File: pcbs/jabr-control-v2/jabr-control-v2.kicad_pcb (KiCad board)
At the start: 6 copper layers, 70 x 80 mm, 245 parts, among them J10001 ARJM11D7-502-AB-EW2, J10002 TYPE-C-31-M-12, J1001 48406-0003, J1002 FH12-22S-0.5SH, J1501 FH12-22S-0.5SH, J1502 FH12-22S-0.5SH, J201 JST-SH-4-Vertical, J4001 MDT320E0X001, J6001 MSPE-J2L0-x00, J9001 43045-0201, Q2602 DMN21D2UFB-7B, SW202 TS20-42-25-WT-160-SMT-TR, U1001 AP22653FDZ-7, U1002 PESD4USB3BTTS-QX, U1003 PESD4USB3BTTS-QX, U1004 PESD4USB3BTTS-QX, U1005 PESD4USB3BTTS-QX, U1201 TPS259472ARPWR, U1301 MAX20004AFOC/VY+T, U1401 TPS62290TDRVRQ1, U1501 TPS62290TDRVRQ1, U201 NX3DV221TKX, U2401 PESD4USB3BTTS-QX, U2402 PESD4USB3BTTS-QX, U301 TVS3301DRBR, U302 TPS26600RHFR, U303 PI7C9X2G304SL, U3801 TPS62290TDRVRQ1, U401 LMQ66430MC3RXBRQ1, U402 TPS7B8133QDRVRQ1, U403 TPS2116DRL, U5001 LAN7431_YXX, U8001 LAN8870, Y401 ASEK-32.768KHZ-LRT, Y8001 XRCGB25M000F3A16R0

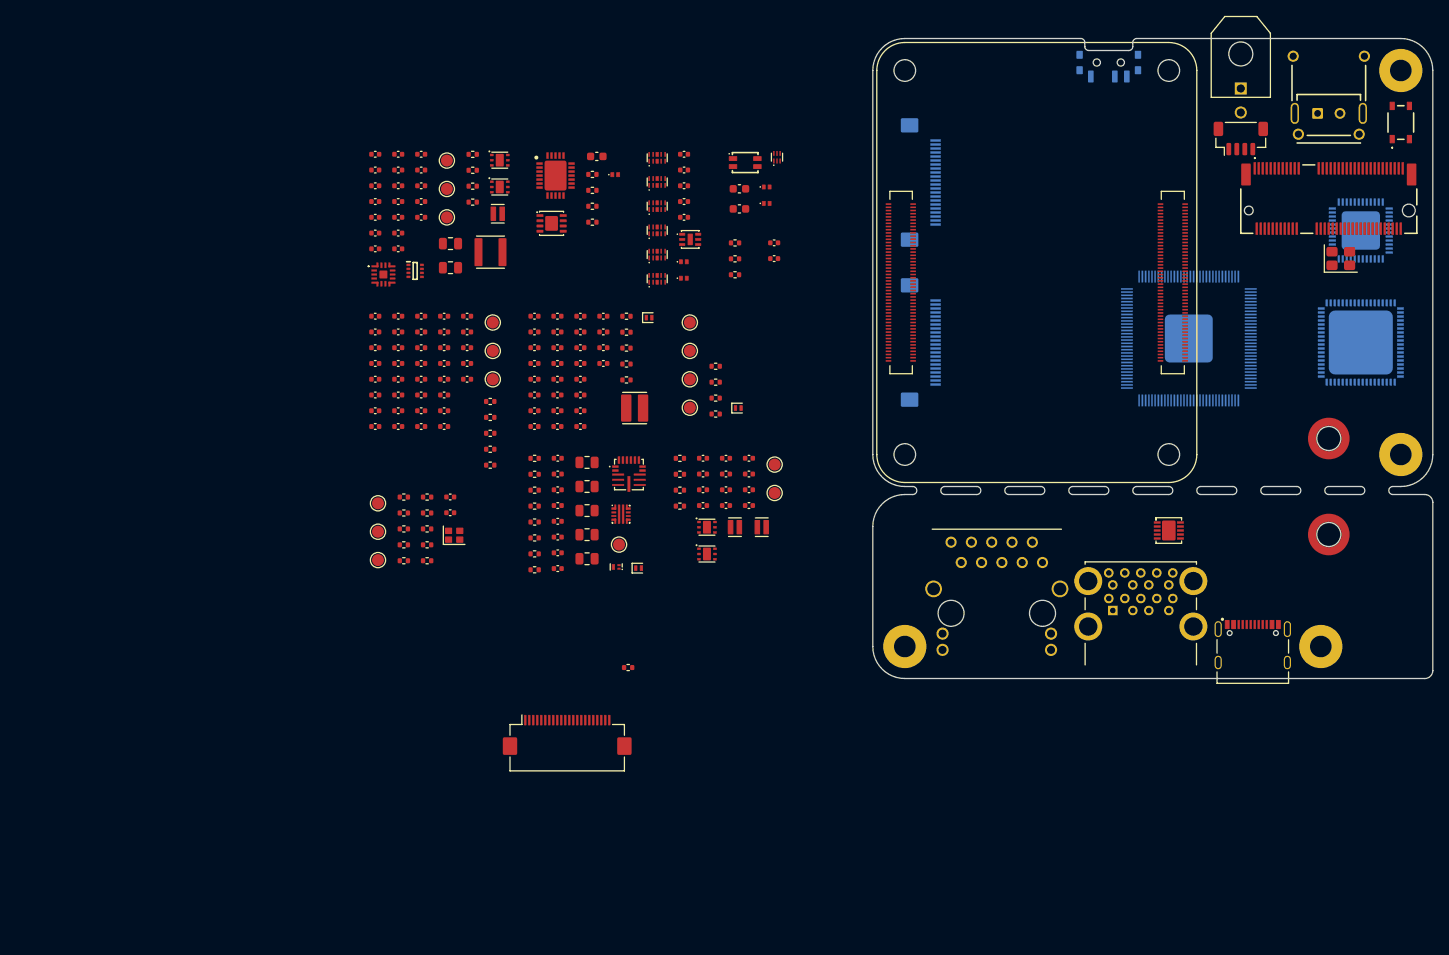
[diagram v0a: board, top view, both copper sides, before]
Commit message: PCI11010 IO done
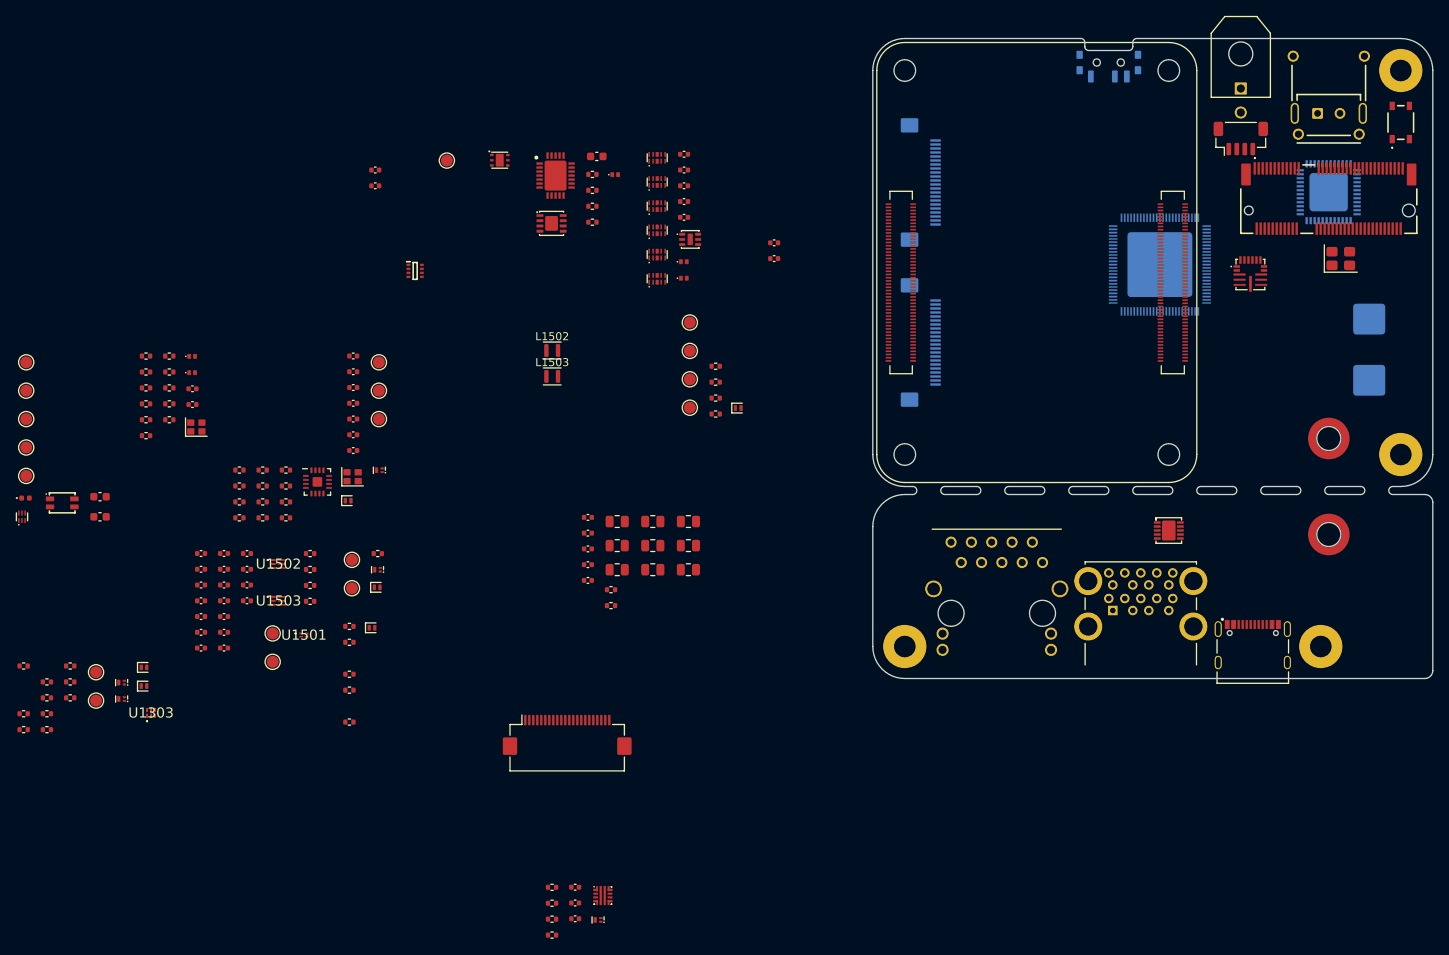
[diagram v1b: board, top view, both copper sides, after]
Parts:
- removed C1401, C1402, C1404, C1405, C1406, C1408, C1409, C1410, C1412, C1413, C1414, C1504, C1505, C1506, C314, C331, C3801, C3802, C3805, C3806, C3807, C406, C407, C501, C512, C513, C514, C515: 4u7, project_footprints:C_0402
- removed the C1403 at (69.7, 77.5)
- removed the C1407 at (69.7, 85.3)
- removed C1411, C3804: 22p, project_footprints:C_0402
- removed the C1503 at (107.8, 119.4)
- removed C2935, C2936: 10p, project_footprints:C_0402
- removed C3001, C3002, C3005, C3006, C3007, C3008, C5001, C5002: 220n, project_footprints:C_0402
- removed C3003, C3004, C308, C309, C310, C311, C312, C313, C315, C316, C317, C318, C319, C320, C321, C322, C323, C324, C325, C326, C327, C328, C329, C330, C503, C504, C505, C506, C507, C509, C510, C511, C516, C517, C518, C519, C520, C521, C522, C523, C524, C525, C526: 100n, project_footprints:C_0402
- removed C401, C402: 10u, project_footprints:C_0805
- removed C403, C502, C508: 1u, project_footprints:C_0402
- removed C601: 100n, project_footprints:C_0603
- removed D2301: PMEG4002EL-QYL, project_footprints:PMEG4002EL-QYL
- removed D302, D601: SZESD7241N2T5G, project_footprints:SZESD7462N2T5G
- removed D303: 824012823, project_footprints:824012823
- removed FL301: ACT1210G-800-2P-TL10, project_footprints:ACT1210G
- removed J6001: MSPE-J2L0-x00, project_footprints:MSPEJ2L0x00
- removed L1401, L1501, L3801: 78438313015, project_footprints:L_Wurth_WE-MAIA-1610
- removed L401: 74479335329222, project_footprints:L_Wurth_WE-PMFI-353220
- removed L501: 74438333033, project_footprints:L_Wurth_WE-MAPI-3010
- removed Q2602: DMN21D2UFB-7B, project_footprints:DMN21D2UFB7B
- removed the R1302 at (86.7, 117.5)
- removed the R1307 at (86.7, 127.4)
- removed the R1308 at (86.7, 129.4)
- removed R1501: 120k, project_footprints:R_0402
- removed R1502, R3802: 180k, project_footprints:R_0402
- removed R3001, R3002: 5k1, project_footprints:R_0402
- removed R318: 475R, project_footprints:R_0402
- removed R319: 1k43, project_footprints:R_0402
- removed R3801: 150k, project_footprints:R_0402
- removed R402, R404, R405, R406, R5004, R5005, R8002, R801, R803, R804, R805, R806, R807, R808, R809: 10k, project_footprints:R_0402
- removed R403: 100k, project_footprints:R_0402
- removed R5001: 200R, project_footprints:R_0402
- removed R5003: 1k5, project_footprints:R_0402
- removed R8001: 12k1, project_footprints:R_0402
- removed the TP1401 at (75.8, 81.8)
- removed TP1402, TP1501, TP3801, TP8001, TP8002, TP801: 1.5mm, project_footprints:TestPoint_Pad_D1.5mm
- removed the U1401 at (82.4, 81.6)
- removed U303: PI7C9X2G304SL, project_footprints:QFP40P1600X1600X160-129N
- removed U3801: TPS62290TDRVRQ1, project_footprints:SON65P200X200X80-7N
- removed U401: LMQ66430MC3RXBRQ1, project_footprints:LMQ664x0
- removed U5001: LAN7431_YXX, project_footprints:QFN50P1000X1000X100-73N-D
- removed U8001: LAN8870, project_footprints:lan8870
- removed Y8001: XRCGB25M000F3A16R0, project_footprints:XRCGB25M000F3A16R0
- added C1314: 22u, project_footprints:C_0805, F.Cu at (101.5, 129.4)
- added C1315: 22u, project_footprints:C_0805, F.Cu at (106.0, 123.4)
- added C1316: 22u, project_footprints:C_0805, F.Cu at (106.0, 126.4)
- added C1317: 22u, project_footprints:C_0805, F.Cu at (106.0, 129.4)
- added C1509: 4u7, project_footprints:C_0402, F.Cu at (45.0, 131.3)
- added C1510: 4u7, project_footprints:C_0402, F.Cu at (45.0, 133.3)
- added C1511: 220p, project_footprints:C_0402, F.Cu at (45.0, 135.3)
- added C1512: 4u7, project_footprints:C_0402, F.Cu at (45.0, 137.2)
- added C1513: 4u7, project_footprints:C_0402, F.Cu at (45.0, 139.2)
- added C1514: 4u7, project_footprints:C_0402, F.Cu at (47.9, 127.4)
- added C1515: 4u7, project_footprints:C_0402, F.Cu at (47.9, 129.3)
- added C1516: 4u7, project_footprints:C_0402, F.Cu at (47.9, 131.3)
- added C1517: 4u7, project_footprints:C_0402, F.Cu at (47.9, 133.3)
- added C1518: 4u7, project_footprints:C_0402, F.Cu at (47.9, 135.3)
- added C1519: 120p, project_footprints:C_0402, F.Cu at (47.9, 137.2)
- added C1520: 4u7, project_footprints:C_0402, F.Cu at (47.9, 139.2)
- added C1521: 4u7, project_footprints:C_0402, F.Cu at (50.8, 127.4)
- added C1522: 4u7, project_footprints:C_0402, F.Cu at (50.8, 129.3)
- added C1523: 4u7, project_footprints:C_0402, F.Cu at (50.8, 131.3)
- added C1524: 4u7, project_footprints:C_0402, F.Cu at (50.8, 133.3)
- added C301: 220n, project_footprints:C_0402, F.Cu at (64.1, 102.7)
- added C701: 10p, project_footprints:C_0402, F.Cu at (44.0, 106.8)
- added C702: 10p, project_footprints:C_0402, F.Cu at (44.0, 108.8)
- added C703: 100n, project_footprints:C_0603, F.Cu at (32.4, 120.3)
- added C704: 100n, project_footprints:C_0603, F.Cu at (32.4, 122.8)
- added D1301: PMEG4002EL-QYL, project_footprints:PMEG4002EL-QYL, F.Cu at (37.9, 141.6)
- added D1302: PMEG4002EL-QYL, project_footprints:PMEG4002EL-QYL, F.Cu at (37.9, 143.9)
- added D201: PMEG4002EL-QYL, project_footprints:PMEG4002EL-QYL, F.Cu at (67.0, 131.6)
- added D301: PMEG4002EL-QYL, project_footprints:PMEG4002EL-QYL, F.Cu at (63.4, 120.8)
- added D701: GREEN, project_footprints:LED_0402, F.Cu at (23.1, 120.4)
- added D702: 824012823, project_footprints:824012823, F.Cu at (22.6, 122.8)
- added D703: SZESD7241N2T5G, project_footprints:SZESD7462N2T5G, F.Cu at (43.9, 102.7)
- added D704: SZESD7241N2T5G, project_footprints:SZESD7462N2T5G, F.Cu at (43.9, 104.8)
- added FL701: ACT1210G-800-2P-TL10, project_footprints:ACT1210G, F.Cu at (27.7, 121.0)
- added J701: MSPE-J2L0-x00, project_footprints:MSPEJ2L0x00, F.Cu at (186.0, 72.4)
- added L1301: 784325078, project_footprints:784325078, B.Cu at (191.1, 101.9)
- added L1502: DFE201610E-R47M=P2, Inductor_SMD:L_Murata_DFE201610P, F.Cu at (88.9, 102.0)
- added L1503: DFE201610E-R47M=P2, Inductor_SMD:L_Murata_DFE201610P, F.Cu at (88.9, 105.2)
- added Q1301: DMN21D2UFB-7B, project_footprints:DMN21D2UFB7B, F.Cu at (94.7, 173.2)
- added Q1302: DMN21D2UFB-7B, project_footprints:DMN21D2UFB7B, F.Cu at (35.1, 143.5)
- added Q1303: DMN21D2UFB-7B, project_footprints:DMN21D2UFB7B, F.Cu at (35.1, 145.6)
- added Q201: DMN21D2UFB-7B, project_footprints:DMN21D2UFB7B, F.Cu at (67.1, 129.4)
- added Q301: DMN21D2UFB-7B, project_footprints:DMN21D2UFB7B, F.Cu at (67.3, 117.0)
- added R1205: 22k, project_footprints:R_0402, F.Cu at (63.6, 148.4)
- added R1301: 100k, project_footprints:R_0402, F.Cu at (22.9, 141.4)
- added R1303: 100k, project_footprints:R_0402, F.Cu at (88.9, 171.1)
- added R1305: 22k, project_footprints:R_0402, F.Cu at (22.9, 147.4)
- added R1309: 47k, project_footprints:R_0402, F.Cu at (88.9, 175.1)
- added R1310: 100k, project_footprints:R_0402, F.Cu at (25.8, 143.4)
- added R1311: 10k, project_footprints:R_0402, F.Cu at (25.8, 145.4)
- added R1312: 10k, project_footprints:R_0402, F.Cu at (25.8, 147.4)
- added R1313: 1M, project_footprints:R_0402, F.Cu at (25.8, 149.4)
- added R1314: 1M, project_footprints:R_0402, F.Cu at (28.7, 141.4)
- added R1315: 4k7, project_footprints:R_0402, F.Cu at (28.7, 143.4)
- added R1316: 4k7, project_footprints:R_0402, F.Cu at (28.7, 145.4)
- added R1504: 47k, project_footprints:R_0402, F.Cu at (58.7, 127.4)
- added R1505: 56k, project_footprints:R_0402, F.Cu at (58.7, 129.4)
- added R1506: 450k, project_footprints:R_0402, F.Cu at (58.7, 131.4)
- added R1507: 100k, project_footprints:R_0402, F.Cu at (58.7, 133.4)
- added R201: 10k, project_footprints:R_0402, F.Cu at (67.1, 127.4)
- added R301: 10k, project_footprints:R_0402, F.Cu at (49.8, 116.9)
- added R302: 10k, project_footprints:R_0402, F.Cu at (49.8, 118.9)
- added R303: 10k, project_footprints:R_0402, F.Cu at (49.8, 120.9)
- added R304: 10k, project_footprints:R_0402, F.Cu at (49.8, 122.9)
- added R307: 10k, project_footprints:R_0402, F.Cu at (52.7, 120.9)
- added R308: 10k, project_footprints:R_0402, F.Cu at (52.7, 122.9)
- added R309: 10k, project_footprints:R_0402, F.Cu at (55.6, 116.9)
- added R310: 100k, project_footprints:R_0402, F.Cu at (55.6, 118.9)
- added R311: 200R, project_footprints:R_0402, F.Cu at (55.6, 120.9)
- added R312: 10k, project_footprints:R_0402, F.Cu at (55.6, 122.9)
- added R502: 10k, project_footprints:R_0402, F.Cu at (63.6, 138.5)
- added R701: 10k, project_footprints:R_0402, F.Cu at (38.2, 102.7)
- added R702: 10k, project_footprints:R_0402, F.Cu at (38.2, 104.7)
- added R703: 10k, project_footprints:R_0402, F.Cu at (38.2, 106.7)
- added R704: 10k, project_footprints:R_0402, F.Cu at (38.2, 108.7)
- added R705: 10k, project_footprints:R_0402, F.Cu at (38.2, 110.7)
- added R706: 12k1, project_footprints:R_0402, F.Cu at (38.2, 112.6)
- added R707: 10k, project_footprints:R_0402, F.Cu at (41.1, 102.7)
- added R708: 10k, project_footprints:R_0402, F.Cu at (41.1, 104.7)
- added R709: 10k, project_footprints:R_0402, F.Cu at (41.1, 106.7)
- added R710: 1k, project_footprints:R_0402, F.Cu at (41.1, 108.7)
- added R711: 10k, project_footprints:R_0402, F.Cu at (41.1, 110.7)
- added TP1302: 1.5mm, project_footprints:TestPoint_Pad_D1.5mm, F.Cu at (31.9, 145.8)
- added TP1502: 1.5mm, project_footprints:TestPoint_Pad_D1.5mm, F.Cu at (54.0, 137.4)
- added TP1503: 1.5mm, project_footprints:TestPoint_Pad_D1.5mm, F.Cu at (54.0, 140.9)
- added TP205: 1.5mm, project_footprints:TestPoint_Pad_D1.5mm, F.Cu at (63.9, 128.2)
- added TP206: 1.5mm, project_footprints:TestPoint_Pad_D1.5mm, F.Cu at (63.9, 131.7)
- added TP701: 1.5mm, project_footprints:TestPoint_Pad_D1.5mm, F.Cu at (23.2, 103.5)
- added TP702: 1.5mm, project_footprints:TestPoint_Pad_D1.5mm, F.Cu at (23.2, 107.0)
- added TP703: 1.5mm, project_footprints:TestPoint_Pad_D1.5mm, F.Cu at (23.2, 110.6)
- added TP704: 1.5mm, project_footprints:TestPoint_Pad_D1.5mm, F.Cu at (23.2, 114.1)
- added TP705: 1.5mm, project_footprints:TestPoint_Pad_D1.5mm, F.Cu at (23.2, 117.7)
- added U1303: AZV3001FZ4-7, project_footprints:AZV3001FZ47, F.Cu at (38.8, 147.3)
- added U1502: TPS62824DMQR, project_footprints:TPS6282xDMQR, F.Cu at (54.7, 128.7)
- added U1503: TPS62824DMQR, project_footprints:TPS6282xDMQR, F.Cu at (54.7, 133.3)
- added U301: SYA75603A, project_footprints:SYA7560x, F.Cu at (59.6, 118.4)
- added U302: PCI11010C, project_footprints:PCI11010C, B.Cu at (164.9, 91.3)
- added U701: LAN8870, project_footprints:lan8870, B.Cu at (186.0, 82.2)
- added Y301: XRCGB25M000F3A16R0, project_footprints:XRCGB25M000F3A16R0, F.Cu at (64.0, 117.8)
- added Y701: XRCGB25M000F3A16R0, project_footprints:XRCGB25M000F3A16R0, F.Cu at (44.4, 111.6)
- C1501: value 4u7 -> 1u
- C1502: value 4u7 -> 100n
- C302: value 100n -> 220n; footprint project_footprints:C_0603 -> project_footprints:C_0402
- C303: value 4u7 -> 220n
- C304: value 100n -> 220n
- C305: value 100n -> 1n
- C306, C307: value 100n -> 10p
- R1304: value 10k -> 12k1
- R1306: value 12k1 -> 10k
- R1401: value 810k -> 47k
- R1402: value 180k -> 22k
- R305: value 10k -> 1k5
- R306: value 330R -> 10k
- U1302: renamed from U1301; value MAX20004AFOC/VY+T -> MAX20008AFOC/VY+T
- U1501: value TPS62290TDRVRQ1 -> TPS22991CNRAAR; footprint project_footprints:SON65P200X200X80-7N -> project_footprints:TPS22991CNRAAR
- moved U1302 81.6 mm to (176.2, 92.5)
- moved R1306 68.2 mm to (22.9, 149.4)
- moved TP1301 67.3 mm to (31.9, 142.2)
- moved C1501 63.9 mm to (45.0, 127.4)
- moved C1502 63.9 mm to (45.0, 129.3)
- moved R1401 62.9 mm to (63.6, 142.5)
- moved R1402 62.9 mm to (63.6, 144.5)
- moved C1307 57.6 mm to (91.8, 173.0)
- moved C302 53.4 mm to (64.1, 104.7)
- moved U1501 52.2 mm to (57.9, 137.6)
- moved R501 52.0 mm to (63.6, 136.5)
- moved D501 52.0 mm to (66.4, 136.7)
- moved R1304 51.7 mm to (88.9, 173.1)
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- renumbered C2401 to C1001, C1004 to C1002, C1001 to C1004, C1002 to C1005, C301 to C1201, C1313 to C1301, C1301 to C1302, C1311 to C1303, C1302 to C1304, C1312 to C1305, C1304 to C1306, C1303 to C1307, C1305 to C1308, C1306 to C1309, C1307 to C1310, C1308 to C1311, C1309 to C1312, C1310 to C1313, C404 to C1403, C405 to C1407, C1507 to C1503, D1002 to D1001, D1001 to D1002, D301 to D1201, D201 to D202, H105 to H102, H102 to H104, H4001 to H401, H4002 to H402, J1002 to J1001, J1001 to J1002, J10001 to J1003, J10002 to J1004, J9001 to J1201, J4001 to J401, R301 to R1201, R302 to R1202, R303 to R1203, R304 to R1204, R1305 to R1302, R1301 to R1307, R1303 to R1308, R201 to R203, R203 to R204, R204 to R205, SOM2001 to SOM201, SW202 to SW201, TP401 to TP1401, TP202 to TP201, TP203 to TP202, TP204 to TP203, TP201 to TP204, U1004 to U1001, U1005 to U1002, U2401 to U1003, U2402 to U1004, U1003 to U1005, U1001 to U1006, U1002 to U1007, U301 to U1201, U302 to U1202, U1201 to U1301, U402 to U1401, U403 to U1404
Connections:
- net /M.2 E-Key/CLK renamed /M.2 E-Key/M2_SPI.CLK
- net /M.2 E-Key/CS renamed /M.2 E-Key/M2_SPI.CS
- net /M.2 E-Key/MISO renamed /M.2 E-Key/M2_SPI.MISO
- net /M.2 E-Key/MOSI renamed /M.2 E-Key/M2_SPI.MOSI
- net /M.2 E-Key/TX renamed /M.2 E-Key/M2_UART.TX
- net /Power/3V3 Regulators/3V3_AON_RAW renamed /Power/3V3 Always On/3V3_AON_RAW
- C1501 pad 1: +5V -> +1V8
- C1502 pad 1: +5V -> +1V8_PCIE
- C302 pad 1: /PCIe to 1000BASE-T1/1000BASE-T1 Connector/CMC_TRXN -> /PCIe Switch/P0_TXN
- C302 pad 2: /PCIe to 1000BASE-T1/1000BASE-T1 Connector/CONN_TRXN -> /CM5/RX_N
- C303 pad 1: +3V3_PCIE -> /PCIe Switch/P1_TXP
- C303 pad 2: GND -> /M.2 E-Key/TX_P
- C304 pad 1: +3V3_PCIE -> /PCIe Switch/P1_TXN
- C304 pad 2: GND -> /M.2 E-Key/TX_N
- C305 pad 1: +3V3_PCIE -> /PCIe Switch/~{RST}
- C306 pad 1: +3V3_PCIE -> GND
- C306 pad 2: GND -> /PCIe Switch/OSC_IN
- C307 pad 1: +3V3_PCIE -> GND
- C307 pad 2: GND -> /PCIe Switch/OSC_OUT
- D501 pad 1: /CM5/~{RST_5V} -> /CM5/~{PCIE_RST}
- D501 pad 2: Net-(D501-A) -> /M.2 Buffers/~{M2_RST}
- J401 pad 15: /M.2 E-Key/~{SPI_INT} -> /M.2 E-Key/M2_SPI.~{INT}
- J401 pad 23: /CM5/~{RST_3V3} -> /M.2 E-Key/M2_SPI.~{RST}
- J401 pad 32: /M.2 E-Key/RX -> /M.2 E-Key/M2_UART.RX
- J401 pad 52: /M.2 E-Key/~{PCIE_RST} -> /M.2 Buffers/~{M2_RST}
- J401 pad 53: /CM5/~{PCIE_CLKREQ} -> /M.2 E-Key/~{PCIE_CLKREQ}
- J401 pad 54: /CM5/BT_EN -> unconnected-(J401-~{W_DISABLE2}-Pad54)
- J401 pad 55: /CM5/~{PCIE_WAKE} -> /M.2 Buffers/~{M2_WAKE}
- J401 pad 56: /CM5/WL_EN -> unconnected-(J401-~{W_DISABLE1}-Pad56)
- J401 pad 58: /CM5/I2C2.SDA -> /M.2 E-Key/M2_I2C.SDA
- J401 pad 60: /CM5/I2C2.SCL -> /M.2 E-Key/M2_I2C.SCL
- J401 pad 62: /M.2 E-Key/~{I2C_INT} -> /M.2 E-Key/M2_I2C.~{INT}
- R1304 pad 1: /PCIe to 1000BASE-T1/INH -> /Power/5V Regulator/OVLO
- R1306 pad 1: /Power/5V Regulator/PGTH -> /1000BASE-T1 PHY/INH
- R1401 pad 1: +3V3_PCIE -> +3V3
- R1401 pad 2: /Power/3V3 Regulators/FB -> /Power/3V3 Always On/PR1
- R1402 pad 1: /Power/3V3 Regulators/FB -> /Power/3V3 Always On/PR1
- R305 pad 1: +3V3_PCIE -> +1V8
- R305 pad 2: /CM5/~{PCIE_RST} -> /1000BASE-T1 PHY/MDIO
- R306 pad 1: /PCIe Switch/PWR_SAV -> +3V3_PCIE
- R306 pad 2: GND -> /CM5/I2C2.SCL
- R501 pad 1: +1V8 -> unconnected-(R501-Pad1)
- R501 pad 2: Net-(D501-A) -> unconnected-(R501-Pad2)
- SOM201 pad 28: unconnected-(SOM2001A-GPIO13-Pad28) -> /CM5/I2C2.SCL
- SOM201 pad 31: unconnected-(SOM2001A-GPIO12-Pad31) -> /CM5/I2C2.SDA
- SOM201 pad 51: unconnected-(SOM2001A-GPIO15-Pad51) -> /CM5/I2C3.SCL
- SOM201 pad 55: unconnected-(SOM2001A-GPIO14-Pad55) -> /CM5/I2C3.SDA
- SOM201 pad 89: /CM5/WL_EN -> unconnected-(SOM201D-WIFI_EN-Pad89)
- SOM201 pad 91: /CM5/BT_EN -> unconnected-(SOM201D-BT_EN-Pad91)
- TP301 pad 1: /PCIe Switch/PORT2_STATUS -> /M.2 E-Key/~{PCIE_CLKREQ}
- TP302 pad 1: /PCIe Switch/PORT1_STATUS -> /PCIe Switch/~{OE1}
- TP303 pad 1: /PCIe Switch/PORT0_STATUS -> /PCIe Switch/LINK
- U1202 pad 22: /Power/Power In/~{FLT} -> unconnected-(U1202-~{FLT}-Pad22)
- U1301 pad 1: VBUS -> /Power/5V Regulator/VBUS_EN
- U1301 pad 12: VBUS -> /Power/5V Regulator/VBUS_EN
- U1301 pad 13: /Power/5V Regulator/PGTH -> unconnected-(U1301-~{FLT}-Pad13)_1
- U1301 pad 2: unconnected-(U1201-OVCSEL-Pad2) -> /Power/5V Regulator/OVLO
- U1301 pad 3: /Power/5V Regulator/VBUS_PG -> unconnected-(U1301-AUXOFF-Pad3)
- U1301 pad 4: /Power/5V Regulator/PGTH -> unconnected-(U1301-~{FLT}-Pad13)
- U1302 pad 11: /Power/5V Regulator/5V_EN -> /Power/5V Regulator/VIN_EN
- U1404 pad 4: /Power/3V3 Regulators/3V3_PG -> /Power/3V3 Always On/PR1
- U1501 pad 1: /Power/1V0 & 1V1 Regulators/SW -> +1V8
- U1501 pad 2: GND -> /CM5/PCIE_PWR_EN
- U1501 pad 3: /Power/1V0 & 1V1 Regulators/FB -> +1V8_PCIE
- U1501 pad 4: +5V -> GND
- U201 pad 6: GND -> /CM5/~{OE}

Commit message: Schematic done
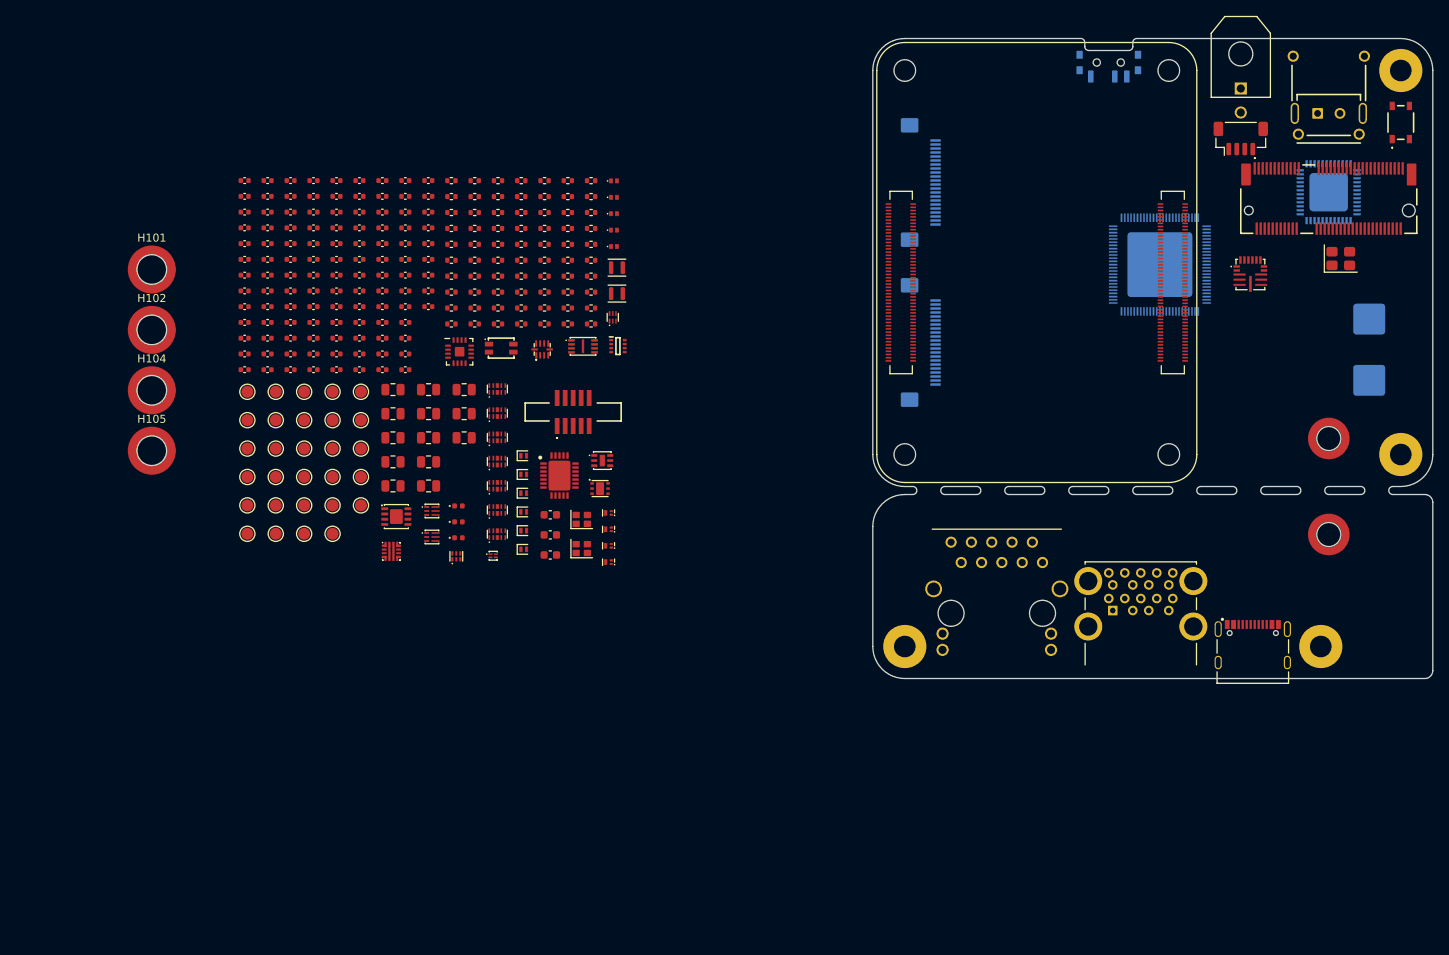
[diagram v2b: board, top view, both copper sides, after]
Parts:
- removed C1003, C1004, C1005, C1503, C1508, C1509, C1510, C1512, C1513, C1514, C1515, C1516, C1517, C1518, C1520, C1521, C1522, C1523, C1524: 4u7, project_footprints:C_0402
- removed C1201, C703, C704: 100n, project_footprints:C_0603
- removed C1301, C1403, C1407, C1501: 1u, project_footprints:C_0402
- removed C1302, C1303, C1312, C1313, C1314, C1315, C1316, C1317: 22u, project_footprints:C_0805
- removed C1304: 4u7, project_footprints:C_0805
- removed C1305, C1307: 2n2, project_footprints:C_0402
- removed C1306, C1309, C1502: 100n, project_footprints:C_0402
- removed C1308: 2u2, project_footprints:C_0402
- removed C1310: 1n, project_footprints:C_0402
- removed C1311: 4p7, project_footprints:C_0402
- removed C1511: 220p, project_footprints:C_0402
- removed C1519: 120p, project_footprints:C_0402
- removed C702: 10p, project_footprints:C_0402
- removed D1001, D1002: SZESD8472MUT5G, project_footprints:SZESD7462N2T5G
- removed D1201: SZESD7241N2T5G, project_footprints:SZESD7462N2T5G
- removed D1301, D1302, D201, D202, D501: PMEG4002EL-QYL, project_footprints:PMEG4002EL-QYL
- removed FL701: ACT1210G-800-2P-TL10, project_footprints:ACT1210G
- removed the J1001 at (90.8, 150.1)
- removed J1004: TYPE-C-31-M-12, project_footprints:TYPE-C-31-M-12
- removed L1502, L1503: DFE201610E-R47M=P2, Inductor_SMD:L_Murata_DFE201610P
- removed Q1301, Q1302, Q1303, Q201, Q301: DMN21D2UFB-7B, project_footprints:DMN21D2UFB7B
- removed R1201: 120k, project_footprints:R_0402
- removed R1202, R1204, R1306, R1311, R1312, R201, R202, R203, R705, R707, R708, R709, R711: 10k, project_footprints:R_0402
- removed R1203, R1315, R1316: 4k7, project_footprints:R_0402
- removed R1205, R1305, R1308, R1402: 22k, project_footprints:R_0402
- removed R1301, R1303, R1310, R1507: 100k, project_footprints:R_0402
- removed R1302: 680R, project_footprints:R_0402
- removed R1304, R1307, R706: 12k1, project_footprints:R_0402
- removed R1309, R1401, R1504: 47k, project_footprints:R_0402
- removed R1313, R1314: 1M, project_footprints:R_0402
- removed R1505: 56k, project_footprints:R_0402
- removed R1506: 450k, project_footprints:R_0402
- removed R204, R205, R710: 1k, project_footprints:R_0402
- removed TP1301, TP1302, TP1401, TP1502, TP1503, TP201, TP202, TP203, TP204, TP205, TP206: 1.5mm, project_footprints:TestPoint_Pad_D1.5mm
- removed U1001, U1002, U1003, U1004, U1005, U1007: PESD4USB3BTTS-QX, project_footprints:PESD4USB3BTTSQX
- removed U1006: AP22653FDZ-7, project_footprints:SON65P200X200X80-7N-D
- removed U1201: TVS3301DRBR, project_footprints:SON65P300X300X100-9N-D
- removed U1202: TPS26600RHFR, project_footprints:QFN50P400X500X100-25N-D
- removed U1301: TPS259472ARPWR, project_footprints:TPS259472ARPWR
- removed U1303: AZV3001FZ4-7, project_footprints:AZV3001FZ47
- removed U1401: TPS7B8133QDRVRQ1, project_footprints:SON65P200X200X80-7N
- removed U1404: TPS2116DRL, project_footprints:SOTFL50P160X60-8N
- removed U1501: TPS22991CNRAAR, project_footprints:TPS22991CNRAAR
- removed U1502, U1503: TPS62824DMQR, project_footprints:TPS6282xDMQR
- removed U201: NX3DV221TKX, project_footprints:SON50P300X300X100-11N
- removed Y701: XRCGB25M000F3A16R0, project_footprints:XRCGB25M000F3A16R0
- added C308: 100n, project_footprints:C_0402, F.Cu at (56.2, 84.7)
- added C309: 100n, project_footprints:C_0402, F.Cu at (53.4, 80.8)
- added C310: 1u, project_footprints:C_0402, F.Cu at (56.2, 86.7)
- added C311: 1u, project_footprints:C_0402, F.Cu at (53.4, 82.7)
- added C312: 1n, project_footprints:C_0402, F.Cu at (56.2, 88.6)
- added C313: 1n, project_footprints:C_0402, F.Cu at (53.4, 84.7)
- added C314: 1n, project_footprints:C_0402, F.Cu at (56.2, 90.6)
- added C315: 220n, project_footprints:C_0402, F.Cu at (50.5, 82.7)
- added C316: 220n, project_footprints:C_0402, F.Cu at (50.5, 84.7)
- added C317: 220n, project_footprints:C_0402, F.Cu at (50.5, 86.7)
- added C318: 220n, project_footprints:C_0402, F.Cu at (50.5, 88.6)
- added C319: 1n, project_footprints:C_0402, F.Cu at (53.4, 86.7)
- added C320: 1n, project_footprints:C_0402, F.Cu at (56.2, 92.6)
- added C321: 1n, project_footprints:C_0402, F.Cu at (53.4, 88.6)
- added C322: 100n, project_footprints:C_0402, F.Cu at (56.2, 94.5)
- added C323: 100n, project_footprints:C_0402, F.Cu at (53.4, 92.6)
- added C324: 1u, project_footprints:C_0402, F.Cu at (56.2, 96.5)
- added C325: 1u, project_footprints:C_0402, F.Cu at (53.4, 94.5)
- added C326: 1n, project_footprints:C_0402, F.Cu at (56.2, 98.5)
- added C327: 1n, project_footprints:C_0402, F.Cu at (53.4, 90.6)
- added C328: 1n, project_footprints:C_0402, F.Cu at (56.2, 100.5)
- added C329: 100n, project_footprints:C_0603, F.Cu at (88.7, 127.6)
- added C330: 1n, project_footprints:C_0402, F.Cu at (53.4, 96.5)
- added C331: 1n, project_footprints:C_0402, F.Cu at (56.2, 102.4)
- added C332: 100n, project_footprints:C_0402, F.Cu at (53.4, 98.5)
- added C333: 100n, project_footprints:C_0402, F.Cu at (56.2, 104.4)
- added C334: 1u, project_footprints:C_0402, F.Cu at (59.1, 80.8)
- added C335: 1n, project_footprints:C_0402, F.Cu at (53.4, 100.5)
- added C336: 100n, project_footprints:C_0402, F.Cu at (53.4, 104.4)
- added C337: 1n, project_footprints:C_0402, F.Cu at (59.1, 82.7)
- added C338: 1n, project_footprints:C_0402, F.Cu at (59.1, 84.7)
- added C339: 1n, project_footprints:C_0402, F.Cu at (59.1, 92.6)
- added C340: 100n, project_footprints:C_0402, F.Cu at (59.1, 86.7)
- added C341: 1n, project_footprints:C_0402, F.Cu at (59.1, 96.5)
- added C342: 100n, project_footprints:C_0402, F.Cu at (59.1, 94.5)
- added C343: 1n, project_footprints:C_0402, F.Cu at (59.1, 88.6)
- added C344: 100n, project_footprints:C_0402, F.Cu at (59.1, 90.6)
- added C345: 1n, project_footprints:C_0402, F.Cu at (59.1, 98.5)
- added C346: 100n, project_footprints:C_0402, F.Cu at (59.1, 100.5)
- added C347: 1n, project_footprints:C_0402, F.Cu at (59.1, 102.4)
- added C348: 100n, project_footprints:C_0402, F.Cu at (59.1, 104.4)
- added C349: 100n, project_footprints:C_0402, F.Cu at (62.0, 80.8)
- added C350: 4u7, project_footprints:C_0402, F.Cu at (62.0, 82.7)
- added C351: 100n, project_footprints:C_0402, F.Cu at (50.5, 96.5)
- added C352: 1n, project_footprints:C_0402, F.Cu at (50.5, 90.6)
- added C353: 10p, project_footprints:C_0402, F.Cu at (50.5, 92.6)
- added C354: 10p, project_footprints:C_0402, F.Cu at (50.5, 94.5)
- added C401: 1u, project_footprints:C_0402, F.Cu at (67.7, 86.7)
- added C402: 22u, project_footprints:C_0805, F.Cu at (69.0, 118.9)
- added C403: 22u, project_footprints:C_0805, F.Cu at (73.5, 106.9)
- added C404: 22u, project_footprints:C_0805, F.Cu at (73.5, 109.9)
- added C405: 22u, project_footprints:C_0805, F.Cu at (73.5, 112.9)
- added C406: 4u7, project_footprints:C_0805, F.Cu at (73.5, 115.9)
- added C407: 100n, project_footprints:C_0402, F.Cu at (67.7, 88.6)
- added C408: 2n2, project_footprints:C_0402, F.Cu at (67.7, 90.6)
- added C409: 2n2, project_footprints:C_0402, F.Cu at (67.7, 92.6)
- added C410: 2u2, project_footprints:C_0402, F.Cu at (67.7, 94.5)
- added C411: 100n, project_footprints:C_0402, F.Cu at (67.7, 96.5)
- added C412: 1n, project_footprints:C_0402, F.Cu at (67.7, 98.5)
- added C413: 4p7, project_footprints:C_0402, F.Cu at (67.7, 100.5)
- added C414: 100n, project_footprints:C_0402, F.Cu at (62.0, 84.7)
- added C415: 22u, project_footprints:C_0805, F.Cu at (73.5, 118.9)
- added C416: 22u, project_footprints:C_0805, F.Cu at (77.9, 106.9)
- added C417: 22u, project_footprints:C_0805, F.Cu at (77.9, 109.9)
- added C418: 22u, project_footprints:C_0805, F.Cu at (77.9, 112.9)
- added C501: 1u, project_footprints:C_0402, F.Cu at (67.7, 102.4)
- added C502: 1u, project_footprints:C_0402, F.Cu at (67.7, 104.4)
- added C601: 4u7, project_footprints:C_0402, F.Cu at (70.6, 80.8)
- added C602: 4u7, project_footprints:C_0402, F.Cu at (70.6, 82.7)
- added C603: 4u7, project_footprints:C_0402, F.Cu at (70.6, 84.7)
- added C604: 4u7, project_footprints:C_0402, F.Cu at (70.6, 86.7)
- added C605: 1u, project_footprints:C_0402, F.Cu at (70.6, 88.6)
- added C606: 100n, project_footprints:C_0402, F.Cu at (70.6, 90.6)
- added C607: 120p, project_footprints:C_0402, F.Cu at (70.6, 94.5)
- added C608: 220p, project_footprints:C_0402, F.Cu at (70.6, 96.5)
- added C609: 4u7, project_footprints:C_0402, F.Cu at (70.6, 98.5)
- added C610: 4u7, project_footprints:C_0402, F.Cu at (70.6, 100.5)
- added C611: 4u7, project_footprints:C_0402, F.Cu at (70.6, 102.4)
- added C612: 4u7, project_footprints:C_0402, F.Cu at (70.6, 104.4)
- added C613: 4u7, project_footprints:C_0402, F.Cu at (73.4, 80.8)
- added C614: 4u7, project_footprints:C_0402, F.Cu at (73.4, 82.7)
- added C615: 4u7, project_footprints:C_0402, F.Cu at (73.4, 94.5)
- added C616: 4u7, project_footprints:C_0402, F.Cu at (73.4, 86.7)
- added C617: 4u7, project_footprints:C_0402, F.Cu at (73.4, 96.5)
- added C618: 4u7, project_footprints:C_0402, F.Cu at (73.4, 90.6)
- added C619: 4u7, project_footprints:C_0402, F.Cu at (73.4, 84.7)
- added C620: 4u7, project_footprints:C_0402, F.Cu at (73.4, 88.6)
- added C801: 100n, project_footprints:C_0402, F.Cu at (64.8, 96.5)
- added C802: 100n, project_footprints:C_0402, F.Cu at (62.0, 96.5)
- added C803: 4u7, project_footprints:C_0402, F.Cu at (64.8, 104.4)
- added C804: 100n, project_footprints:C_0402, F.Cu at (62.0, 98.5)
- added C805: 100n, project_footprints:C_0402, F.Cu at (62.0, 100.5)
- added C806: 100n, project_footprints:C_0402, F.Cu at (62.0, 90.6)
- added C807: 1u, project_footprints:C_0402, F.Cu at (62.0, 102.4)
- added C808: 1u, project_footprints:C_0402, F.Cu at (62.0, 92.6)
- added C809: 4u7, project_footprints:C_0402, F.Cu at (62.0, 104.4)
- added C810: 100n, project_footprints:C_0402, F.Cu at (62.0, 94.5)
- added C811: 100n, project_footprints:C_0402, F.Cu at (64.8, 80.8)
- added C812: 100n, project_footprints:C_0402, F.Cu at (64.8, 98.5)
- added C813: 100n, project_footprints:C_0402, F.Cu at (64.8, 82.7)
- added C814: 100n, project_footprints:C_0402, F.Cu at (64.8, 100.5)
- added C815: 100n, project_footprints:C_0402, F.Cu at (64.8, 84.7)
- added C816: 4u7, project_footprints:C_0402, F.Cu at (64.8, 102.4)
- added C817: 1u, project_footprints:C_0402, F.Cu at (64.8, 86.7)
- added C818: 100n, project_footprints:C_0402, F.Cu at (64.8, 88.6)
- added C819: 100n, project_footprints:C_0402, F.Cu at (64.8, 90.6)
- added C820: 100n, project_footprints:C_0402, F.Cu at (64.8, 92.6)
- added C821: 10p, project_footprints:C_0402, F.Cu at (62.0, 86.7)
- added C822: 10p, project_footprints:C_0402, F.Cu at (62.0, 88.6)
- added C823: 4u7, project_footprints:C_0402, F.Cu at (64.8, 94.5)
- added C824: 100n, project_footprints:C_0603, F.Cu at (88.7, 122.5)
- added C825: 100n, project_footprints:C_0603, F.Cu at (88.7, 125.0)
- added C901: 100n, project_footprints:C_0402, F.Cu at (67.7, 80.8)
- added C902: 22u, project_footprints:C_0805, F.Cu at (69.0, 109.9)
- added C903: 22u, project_footprints:C_0805, F.Cu at (69.0, 112.9)
- added C904: 22u, project_footprints:C_0805, F.Cu at (69.0, 115.9)
- added C905: 22u, project_footprints:C_0805, F.Cu at (69.0, 106.9)
- added C906: 4u7, project_footprints:C_0402, F.Cu at (67.7, 82.7)
- added C907: 4u7, project_footprints:C_0402, F.Cu at (67.7, 84.7)
- added D302: SZESD7241N2T5G, project_footprints:SZESD7462N2T5G, F.Cu at (96.6, 89.0)
- added D401: PMEG4002EL-QYL, project_footprints:PMEG4002EL-QYL, F.Cu at (85.4, 124.5)
- added D402: PMEG4002EL-QYL, project_footprints:PMEG4002EL-QYL, F.Cu at (85.4, 126.9)
- added D705: RED, project_footprints:LED_0402, F.Cu at (77.2, 123.4)
- added D801: GREEN, project_footprints:LED_0402, F.Cu at (77.2, 125.4)
- added D802: 824012823, project_footprints:824012823, F.Cu at (96.5, 97.9)
- added D803: SZESD7241N2T5G, project_footprints:SZESD7462N2T5G, F.Cu at (96.6, 80.8)
- added D804: SZESD7241N2T5G, project_footprints:SZESD7462N2T5G, F.Cu at (96.6, 82.8)
- added D901: SZESD8472MUT5G, project_footprints:SZESD7462N2T5G, F.Cu at (96.6, 84.9)
- added D902: SZESD8472MUT5G, project_footprints:SZESD7462N2T5G, F.Cu at (96.6, 87.0)
- added FL801: ACT1210G-800-2P-TL10, project_footprints:ACT1210G, F.Cu at (82.5, 101.7)
- added H101: 9774015951R, Mounting_Wuerth:Mounting_Wuerth_WA-SMST-2.7mm_H1.5mm_9774015951, F.Cu at (38.9, 91.9)
- added H102: 9774015951R, Mounting_Wuerth:Mounting_Wuerth_WA-SMST-2.7mm_H1.5mm_9774015951, F.Cu at (38.9, 99.4)
- added H104: 9774015951R, Mounting_Wuerth:Mounting_Wuerth_WA-SMST-2.7mm_H1.5mm_9774015951, F.Cu at (38.9, 107.0)
- added H105: 9774015951R, Mounting_Wuerth:Mounting_Wuerth_WA-SMST-2.7mm_H1.5mm_9774015951, F.Cu at (38.9, 114.5)
- added J701: FFC3A20-05-G, project_footprints:FFC3A2005G, F.Cu at (91.5, 109.7)
- added J903: TYPE-C-31-M-12, project_footprints:TYPE-C-31-M-12, F.Cu at (176.5, 141.0)
- added L601: DFE201610E-R47M=P2, Inductor_SMD:L_Murata_DFE201610P, F.Cu at (97.0, 91.6)
- added L602: DFE201610E-R47M=P2, Inductor_SMD:L_Murata_DFE201610P, F.Cu at (97.0, 94.9)
- added Q401: DMN21D2UFB-7B, project_footprints:DMN21D2UFB7B, F.Cu at (96.0, 124.4)
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- renumbered H102 to H103, H104 to H106, H101 to H107, H103 to H108, J1501 to J1001, J1502 to J1002, J1201 to J301, J201 to J702, J701 to J801, J1002 to J901, J1003 to J902, L1301 to L401, S201 to S701, SOM201 to SOM701, SW201 to SW701, U302 to U303, U1302 to U403, U701 to U801
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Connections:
- C1001 pad 1: /CM5IO/CT -> +3V3
- C1002 pad 1: /CM5IO/VBUS_OUT -> +3V3
- C301 pad 1: /PCIe Switch/P0_TXP -> +1V1
- C301 pad 2: /CM5/RX_P -> GND
- C302 pad 1: /PCIe Switch/P0_TXN -> +3V3_PCIE
- C302 pad 2: /CM5/RX_N -> GND
- C303 pad 1: /PCIe Switch/P1_TXP -> +1V1
- C303 pad 2: /M.2 E-Key/TX_P -> GND
- C304 pad 1: /PCIe Switch/P1_TXN -> +3V3_PCIE
- C304 pad 2: /M.2 E-Key/TX_N -> GND
- C305 pad 1: /PCIe Switch/~{RST} -> +1V1
- C306 pad 1: GND -> +3V3_PCIE
- C306 pad 2: /PCIe Switch/OSC_IN -> GND
- C307 pad 1: GND -> +1V1
- C307 pad 2: /PCIe Switch/OSC_OUT -> GND
- C701 pad 1: GND -> +3V3
- C701 pad 2: /1000BASE-T1 PHY/OSC_IN -> GND
- D301 pad 1: /CM5/~{RST_5V} -> /PCIe Switch/~{PORT1_CLKREQ}
- D301 pad 2: /PCIe Switch/~{RST} -> /PCIe Switch/~{OE0}
- D701 pad 1: /1000BASE-T1 PHY/LINK_LED -> /CM5/NRST
- D701 pad 2: +1V8 -> /CM5/NRST_CONN
- D702 pad 1: /1000BASE-T1 PHY/TRXN -> /CM5/~{PERST}
- D702 pad 2: /1000BASE-T1 PHY/TRXP -> /CM5/~{PCIE_RST}
- D703 pad 1: GND -> /CM5/~{BOOT}
- D703 pad 2: /1000BASE-T1 PHY/CONN_TRXP -> /CM5/~{OE}
- D704 pad 1: GND -> /CM5/~{LED_ACT}
- D704 pad 2: /1000BASE-T1 PHY/CONN_TRXN -> /CM5/~{LED_ACT_A}
- J1001 pad 20: /CM5/I2C1.SDA -> /CM5/MIPI0.SCL
- J1001 pad 21: /CM5/I2C1.SCL -> /CM5/MIPI0.SDA
- J1002 pad 17: Net-(J1502-Pad17) -> /MIPI Connectors/~{MIPI1_RST}
- J1002 pad 20: /CM5/I2C0.SCL -> /CM5/MIPI1.SCL
- J1002 pad 21: /CM5/I2C0.SDA -> /CM5/MIPI1.SDA
- J401 pad 2: +3V3_M2 -> +3V3_PCIE
- J401 pad 22: /M.2 E-Key/M2_UART.TX -> /M.2 E-Key/M2_UART.RX
- J401 pad 23: /M.2 E-Key/M2_SPI.~{RST} -> unconnected-(J401-~{SDIO_RESET}-Pad23)
- J401 pad 32: /M.2 E-Key/M2_UART.RX -> /M.2 E-Key/M2_UART.TX
- J401 pad 4: +3V3_M2 -> +3V3_PCIE
- J401 pad 52: /M.2 Buffers/~{M2_RST} -> /CM5/~{PCIE_RST}
- J401 pad 53: /M.2 E-Key/~{PCIE_CLKREQ} -> /PCIe Switch/~{PORT1_CLKREQ}
- J401 pad 55: /M.2 Buffers/~{M2_WAKE} -> /CM5/~{PCIE_WAKE}
- J401 pad 72: +3V3_M2 -> +3V3_PCIE
- J401 pad 74: +3V3_M2 -> +3V3_PCIE
- R301 pad 1: +1V8 -> +3V3_PCIE
- R301 pad 2: /M.2 E-Key/~{PCIE_CLKREQ} -> /PCIe Switch/~{PORT1_CLKREQ}
- R302 pad 1: +3V3_PCIE -> +1V8_PCIE
- R302 pad 2: /CM5/I2C2.~{INT} -> /PCIe Switch/~{OE0}
- R303 pad 1: /PCIe Switch/EEPROM_STRAP -> +3V3_PCIE
- R303 pad 2: GND -> /M.2 E-Key/M2_I2C.~{INT}
- R304 pad 1: +1V8 -> +3V3_PCIE
- R304 pad 2: /1000BASE-T1 PHY/~{RST} -> /M.2 E-Key/M2_I2C.SCL
- R305 pad 1: +1V8 -> /PCIe Switch/VAUX_DET
- R305 pad 2: /1000BASE-T1 PHY/MDIO -> GND
- R306 pad 2: /CM5/I2C2.SCL -> /M.2 E-Key/M2_I2C.SDA
- R307 pad 2: /CM5/I2C2.SDA -> /CM5/~{PCIE_RST}
- R308 pad 1: +1V8 -> /Power/Power In/VIN_RAW
- R308 pad 2: /PCIe Switch/LINK -> /Power/Power In/UVLO
- R309 pad 1: +3V3_PCIE -> /Power/Power In/UVLO
- R309 pad 2: Net-(U302A-PROG68/SERIAL_SEL_STRAP) -> /Power/Power In/OVP
- R310 pad 1: /PCIe Switch/TESTEN -> /Power/Power In/OVP
- R310 pad 2: GND -> /Power/Power In/RTN
- R311 pad 1: /PCIe Switch/ENET_RESREF -> +1V8_PCIE
- R311 pad 2: GND -> /1000BASE-T1 PHY/~{RST}
- R312 pad 1: +3V3_PCIE -> /M.2 E-Key/M2_SPI.MISO
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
